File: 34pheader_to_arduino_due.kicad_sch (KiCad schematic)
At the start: 5 parts, among them J1 Conn_02x17_Odd_Even, J2 Conn_02x17_Odd_Even, J3 Conn_01x02_Pin, J4 Conn_01x02_Pin, J5 Conn_01x02_Pin

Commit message: Continue on board design
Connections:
- net at J1.14 (Pin_14), J2.2 (Pin_2): now also J1.16 (Pin_16), J2.1 (Pin_1)
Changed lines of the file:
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@@
 (kicad_sch (version 20230121) (generator eeschema)
   (paper "A4")
+  (junction (at 127 86.36) (diameter 0) (color 0 0 0 0)
+  )
+  (junction (at 125.73 86.36) (diameter 0) (color 0 0 0 0)
+  )
   (no_connect (at 152.4 82.55))
   (no_connect (at 123.19 58.42))
@@
   (no_connect (at 120.65 99.06))
   (wire (pts (xy 165.1 66.04) (xy 165.1 67.31))
+    (stroke (width 0) (type default))
+  )
+  (wire (pts (xy 127 86.36) (xy 127 81.28))
     (stroke (width 0) (type default))
   )
@@
     (stroke (width 0) (type default))
   )
-  (wire (pts (xy 125.73 78.74) (xy 125.73 102.87))
+  (wire (pts (xy 125.73 78.74) (xy 125.73 86.36))
     (stroke (width 0) (type default))
   )
@@
     (stroke (width 0) (type default))
   )
+  (wire (pts (xy 125.73 86.36) (xy 127 86.36))
+    (stroke (width 0) (type default))
+  )
   (wire (pts (xy 134.62 64.77) (xy 152.4 64.77))
     (stroke (width 0) (type default))
   )
-  (wire (pts (xy 127 100.33) (xy 127 81.28))
+  (wire (pts (xy 127 100.33) (xy 127 86.36))
     (stroke (width 0) (type default))
   )
@@
     (stroke (width 0) (type default))
   )
+  (wire (pts (xy 125.73 86.36) (xy 125.73 102.87))
+    (stroke (width 0) (type default))
+  )

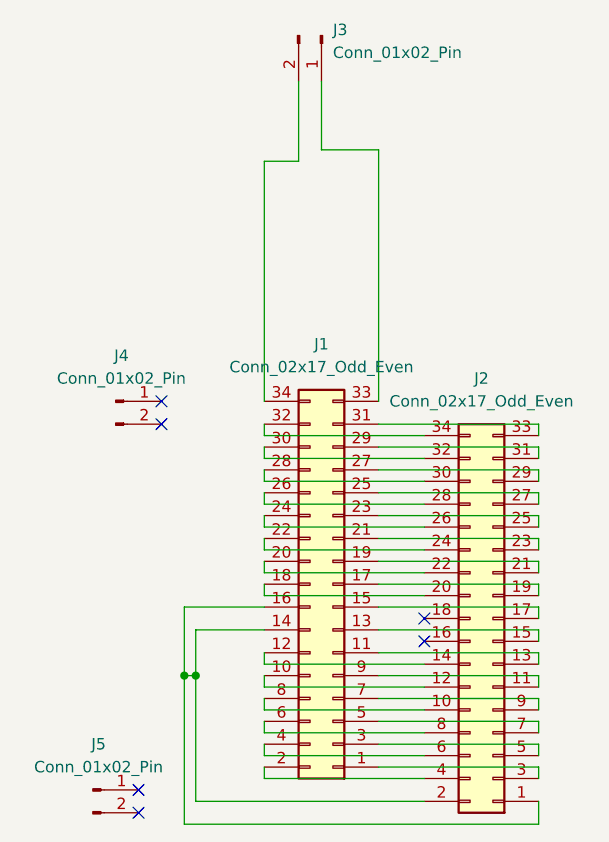
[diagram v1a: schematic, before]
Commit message: Ensure pinout is correct
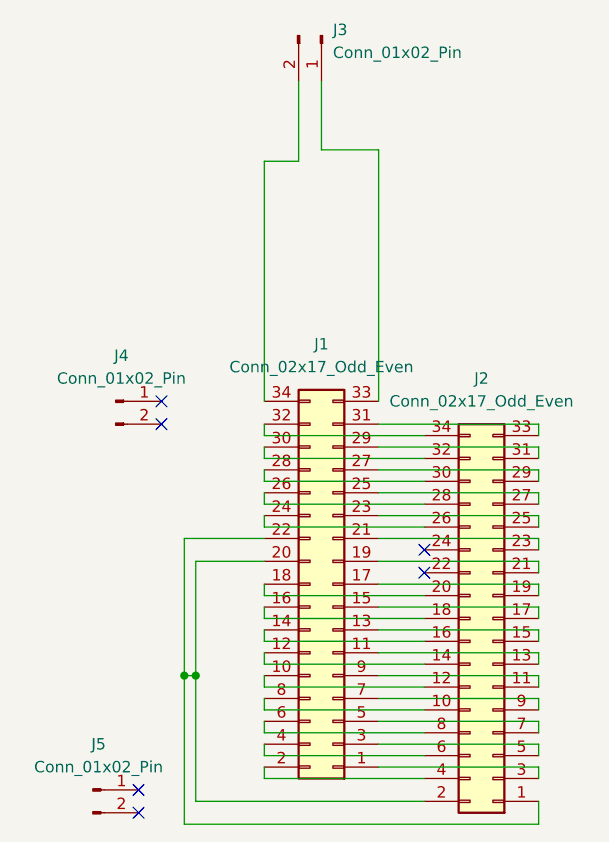
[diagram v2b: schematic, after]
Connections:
- net at J2.1 (Pin_1), J2.2 (Pin_2): now also J1.20 (Pin_20), J1.22 (Pin_22); no longer J1.14 (Pin_14), J1.16 (Pin_16)
- net at J2.22 (Pin_22): no longer J1.20 (Pin_20)
- net at J2.24 (Pin_24): no longer J1.22 (Pin_22)
- net at J2.16 (Pin_16): now also J1.14 (Pin_14)
- net at J2.18 (Pin_18): now also J1.16 (Pin_16)
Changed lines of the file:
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@@
   (junction (at 125.73 86.36) (diameter 0) (color 0 0 0 0)
   )
-  (no_connect (at 152.4 82.55))
+  (no_connect (at 152.4 72.39))
   (no_connect (at 123.19 58.42))
-  (no_connect (at 152.4 80.01))
+  (no_connect (at 152.4 74.93))
   (no_connect (at 120.65 101.6))
   (no_connect (at 123.19 55.88))
@@
     (stroke (width 0) (type default))
   )
-  (wire (pts (xy 127 86.36) (xy 127 81.28))
+  (wire (pts (xy 134.62 81.28) (xy 134.62 82.55))
+    (stroke (width 0) (type default))
+  )
+  (wire (pts (xy 127 73.66) (xy 127 86.36))
     (stroke (width 0) (type default))
   )
@@
     (stroke (width 0) (type default))
   )
-  (wire (pts (xy 125.73 78.74) (xy 125.73 86.36))
+  (wire (pts (xy 125.73 71.12) (xy 125.73 86.36))
     (stroke (width 0) (type default))
   )
@@
     (stroke (width 0) (type default))
   )
-  (wire (pts (xy 134.62 73.66) (xy 134.62 74.93))
-    (stroke (width 0) (type default))
-  )
   (wire (pts (xy 147.32 68.58) (xy 165.1 68.58))
     (stroke (width 0) (type default))
@@
     (stroke (width 0) (type default))
   )
+  (wire (pts (xy 127 73.66) (xy 134.62 73.66))
+    (stroke (width 0) (type default))
+  )
   (wire (pts (xy 147.32 91.44) (xy 165.1 91.44))
     (stroke (width 0) (type default))
@@
     (stroke (width 0) (type default))
   )
-  (wire (pts (xy 127 81.28) (xy 134.62 81.28))
-    (stroke (width 0) (type default))
-  )
   (wire (pts (xy 147.32 60.96) (xy 165.1 60.96))
     (stroke (width 0) (type default))
@@
     (stroke (width 0) (type default))
   )
+  (wire (pts (xy 134.62 82.55) (xy 152.4 82.55))
+    (stroke (width 0) (type default))
+  )
   (wire (pts (xy 138.43 20.32) (xy 138.43 29.21))
     (stroke (width 0) (type default))
@@
     (stroke (width 0) (type default))
   )
-  (wire (pts (xy 134.62 71.12) (xy 134.62 72.39))
-    (stroke (width 0) (type default))
-  )
   (wire (pts (xy 134.62 66.04) (xy 134.62 67.31))
     (stroke (width 0) (type default))
@@
     (stroke (width 0) (type default))
   )
+  (wire (pts (xy 125.73 71.12) (xy 134.62 71.12))
+    (stroke (width 0) (type default))
+  )
   (wire (pts (xy 147.32 81.28) (xy 165.1 81.28))
     (stroke (width 0) (type default))
@@
     (stroke (width 0) (type default))
   )
-  (wire (pts (xy 125.73 78.74) (xy 134.62 78.74))
-    (stroke (width 0) (type default))
-  )
-  (wire (pts (xy 134.62 72.39) (xy 152.4 72.39))
-    (stroke (width 0) (type default))
-  )
   (wire (pts (xy 165.1 91.44) (xy 165.1 92.71))
     (stroke (width 0) (type default))
@@
     (stroke (width 0) (type default))
   )
-  (wire (pts (xy 134.62 74.93) (xy 152.4 74.93))
-    (stroke (width 0) (type default))
-  )
   (wire (pts (xy 147.32 78.74) (xy 165.1 78.74))
     (stroke (width 0) (type default))
@@
     (stroke (width 0) (type default))
   )
+  (wire (pts (xy 134.62 80.01) (xy 152.4 80.01))
+    (stroke (width 0) (type default))
+  )
   (wire (pts (xy 147.32 96.52) (xy 165.1 96.52))
     (stroke (width 0) (type default))
@@
     (stroke (width 0) (type default))
   )
+  (wire (pts (xy 134.62 78.74) (xy 134.62 80.01))
+    (stroke (width 0) (type default))
+  )
